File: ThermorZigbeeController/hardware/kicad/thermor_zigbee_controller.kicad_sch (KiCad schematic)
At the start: 3 parts, among them U1 ESP32-C6-WROOM-1, U2 HT1621, U3 PC817

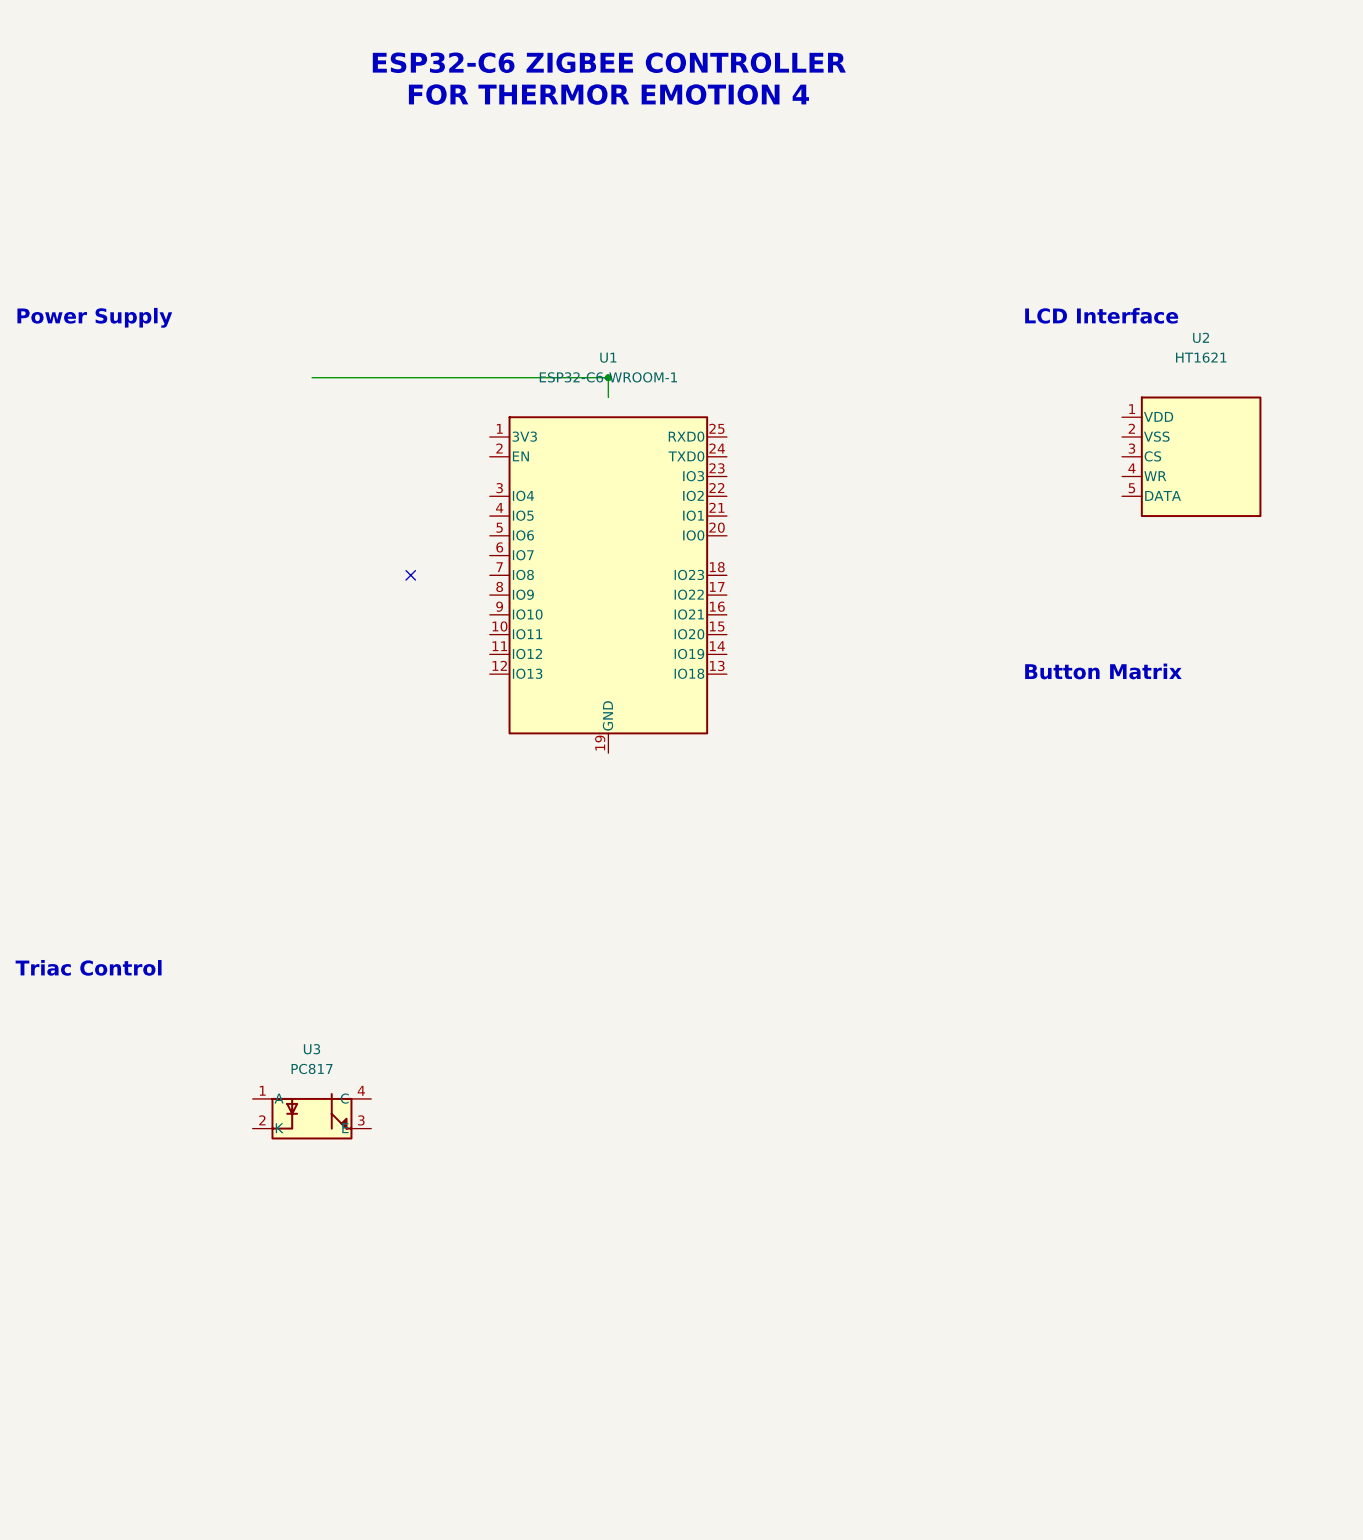
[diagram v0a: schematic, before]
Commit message: fix: Complete missing files and add PIR sensor support
- Fix KiCad schema syntax errors (justify parameter)
- Add PIR HC-SR501 presence sensor to hardware design (GPIO7)
- Create missing thermor_zigbee.h/c core files
- Add comprehensive PIR integration guide
- Create PIR sensor test suite
- Update CMakeLists.txt with all source files

The presence detection is now fully integrated with automatic
comfort/eco mode switching based on room occupancy.

🤖 Generated with Claude Code

Co-Authored-By: Claude <noreply@anthropic.com>
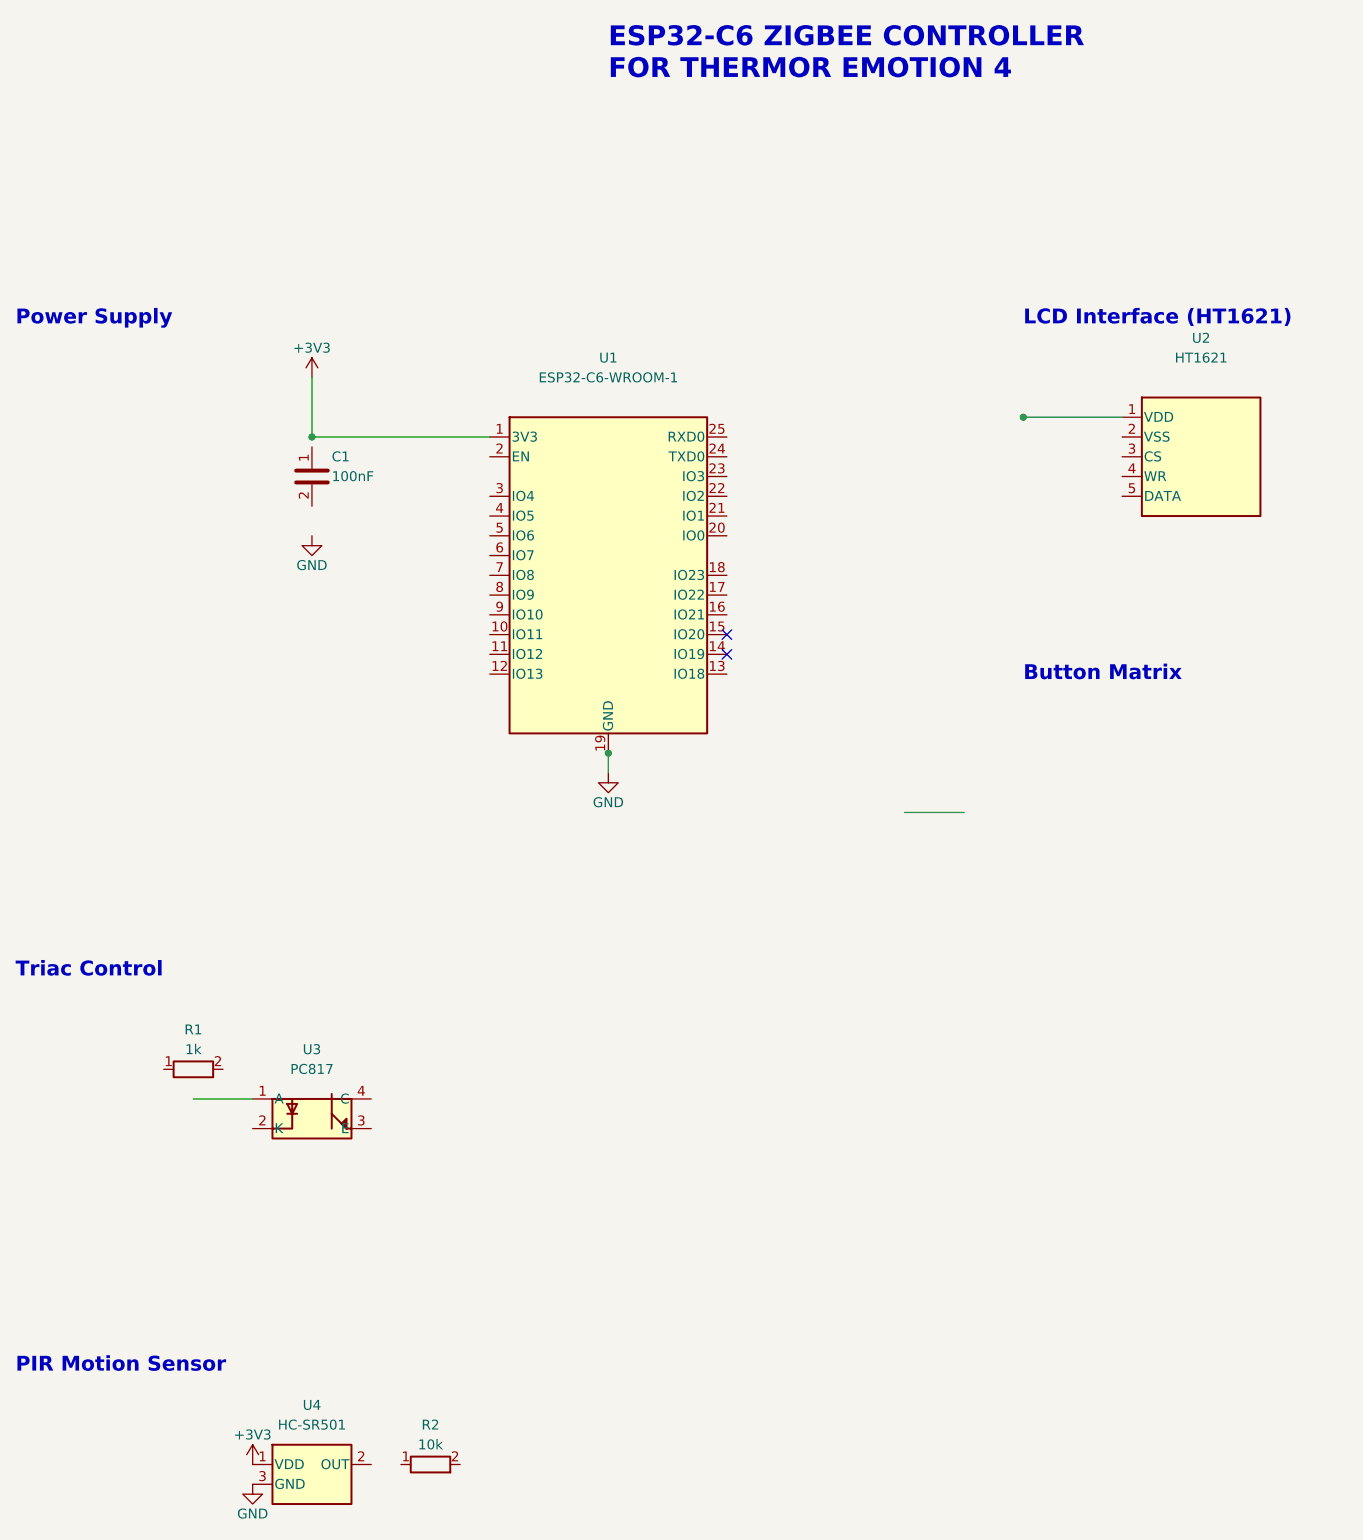
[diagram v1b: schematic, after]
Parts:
- added C1: 100nF, Capacitor_SMD:C_0603_1608Metric, symbol Device:C
- added R1: 1k, Resistor_SMD:R_0603_1608Metric, symbol Device:R
- added R2: 10k, Resistor_SMD:R_0603_1608Metric, symbol Device:R
- added U4: HC-SR501, symbol PIR_Sensor
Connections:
- net +3V3: now reaches U1.1 (3V3)
- net +3V3: now also U4.1 (VDD)
- net GND: now reaches U1.19 (GND)
- net GND: now also U4.3 (GND)
- no-connect marks 1 -> 2
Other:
- note added: "LCD Interface (HT1621)"
- note added: "PIR Motion Sensor"
- note removed: "LCD Interface"
